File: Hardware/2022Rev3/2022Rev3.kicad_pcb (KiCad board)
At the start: 2 copper layers, 114.3 x 124.5 mm, 101 parts, among them J1 Conn_01x04, J2 Conn_01x06, J3 RJ45_LED_Shielded, J4 Conn_01x09, J5 Conn_01x09, J6 Conn_01x03, Q1 Q_NMOS_DGS, Q2 Q_NMOS_DGS, SW1 SW_SPDT, U1 ACS758xCB-200B-PFF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

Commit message: layout changes
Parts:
- removed C8: 0.1uF, Capacitor_SMD:C_0603_1608Metric_Pad1.08x0.95mm_HandSolder
- removed J2: Conn_01x06, Connector_PinHeader_2.00mm:PinHeader_2x03_P2.00mm_Vertical
- removed J3: RJ45_LED_Shielded, MRDT_Connectors:RJ45_Teensy
- added G***: LOGO, businessCards:logo, F.Cu at (181.5, 145.8)
- added G***: LOGO, MRDT_Silkscreens:0_MRDT_Logo_30mm, F.Cu at (179.3, 86.2)
- added G***: LOGO, MRDT_Silkscreens:z_sig_MaxRyan_25x6.6mm, F.Cu at (252.2, 122.9)
- moved BZ1 10.0 mm to (227.5, 157.7)
- moved D12 9.14 mm to (220.8, 140.0)
- moved Q2 9.14 mm to (207.1, 159.2)
- moved R39 9.14 mm to (207.0, 155.6)
- moved R43 9.14 mm to (217.0, 140.0)
- moved U5 9.14 mm to (181.9, 145.5)
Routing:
- net CURRENT_SENSE: track 13.4 -> 139.0 mm
- net cell7-sense: track 25.5 -> 16.4 mm
- net cell6-sense: track 34.2 -> 25.0 mm
- net cell4-sense: track 49.1 -> 39.9 mm
- net cell3-sense: track 56.2 -> 47.0 mm
- net cell2-sense: track 64.0 -> 54.8 mm
- net cell1-sense: track 70.9 -> 61.8 mm
- net cell5-sense: track 41.8 -> 32.6 mm
- net TEMP_SENSE: track 62.5 -> 71.3 mm
- net cell8-sense: track 21.5 -> 12.8 mm
- net +3V3: track 91.6 -> 99.0 mm
- net PACK_OUT_SENSE: track 88.1 -> 95.4 mm
- net +5V: track 165.1 -> 159.4 mm, vias 10 -> 9
- net GATE: track 79.9 -> 85.0 mm
- net GND: vias 68 -> 70
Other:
- board text added: "Battery Management System, Rev3 Mars Rover Design Team, 2022 Missouri S&T Maxwell Ryan"
- board text added: "GND"
- board text added: "V IN"
- board text added: "V OUT"

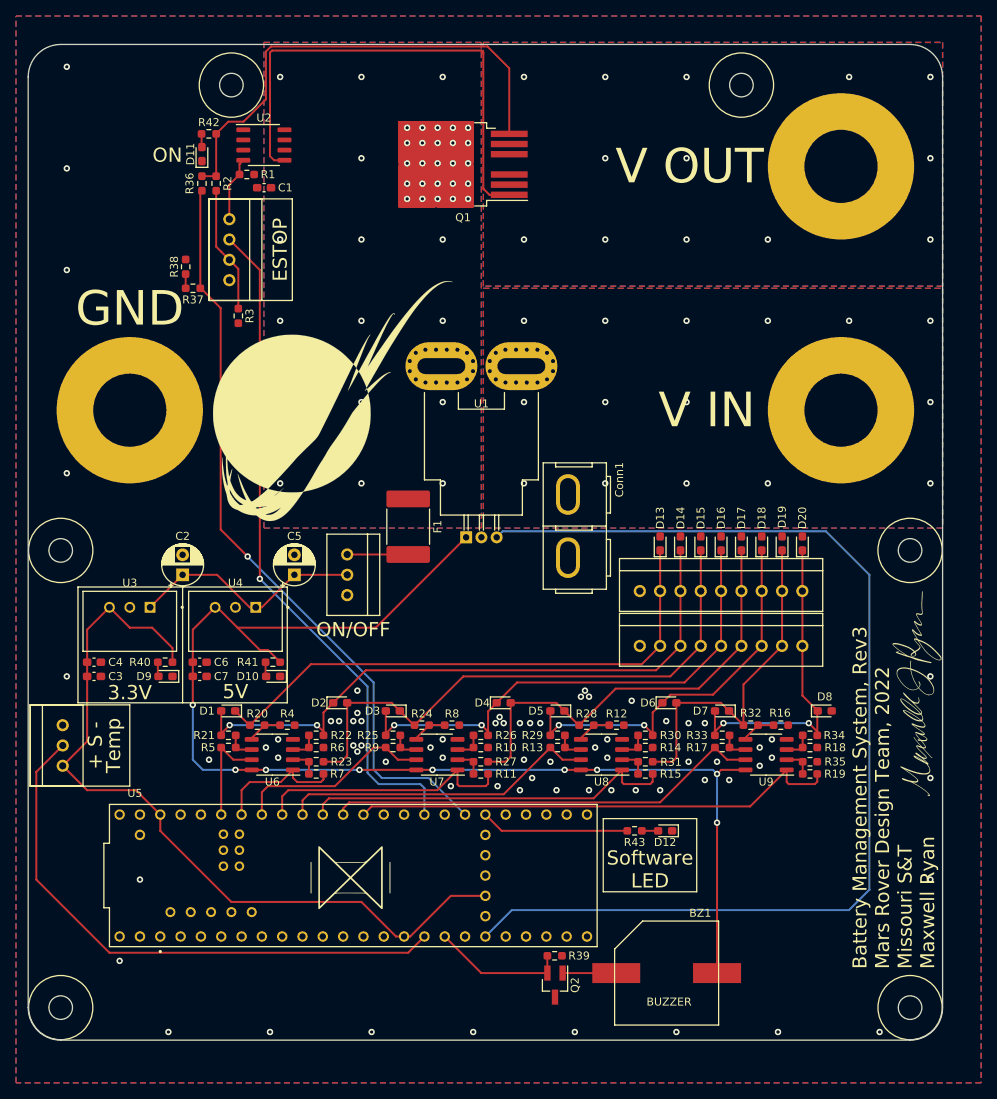
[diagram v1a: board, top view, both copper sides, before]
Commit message: Added fan circuit
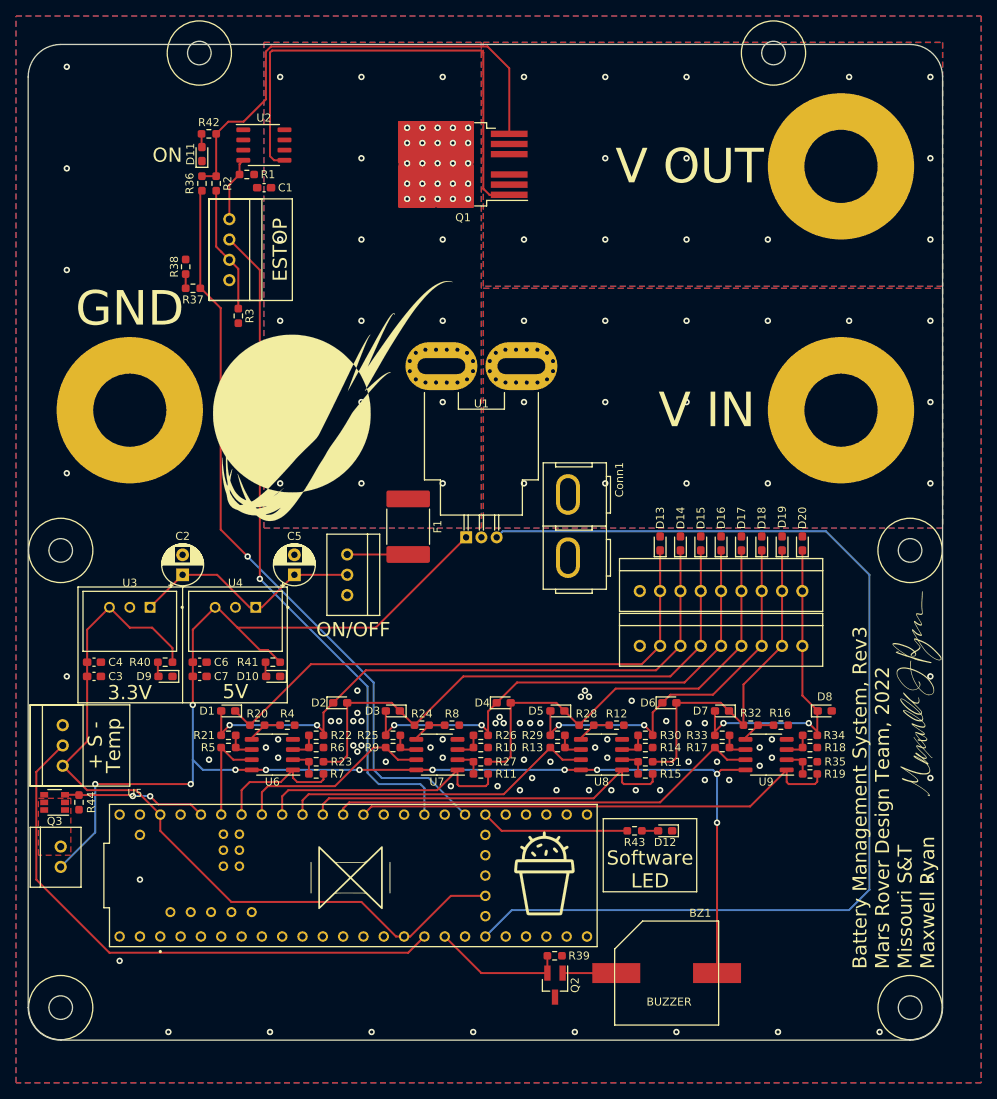
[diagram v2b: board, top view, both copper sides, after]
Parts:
- added Conn2: Molex_SL_02, MRDT_Connectors:MOLEX_SL_02_Vertical, F.Cu at (145.3, 144.5)
- added G***: LOGO, MRDT_Silkscreens:z_sig_Alex_Wortmann_PT2, F.Cu at (205.7, 145.5)
- added Q3: Q_NMOS_DSG, Package_TO_SOT_SMD:SuperSOT-6, F.Cu at (144.5, 136.4)
- added R44: 820, Resistor_SMD:R_0603_1608Metric_Pad0.98x0.95mm_HandSolder, F.Cu at (147.6, 136.4)
- H2, H3: footprint MRDT_Drill_Holes:4_40_Hole -> MRDT_Drill_Holes:4_40_Hole_Corner
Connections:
- U5 pad 22: unconnected-(U5-Pad22) -> Fan_CTRL
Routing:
- net +5V: track 159.4 -> 186.6 mm, vias 9 -> 11
- net Fan_CTRL: track 0.00 -> 18.0 mm, vias 0 -> 2
- added copper zone on F.Cu, net Net-(Q3-Pad1)
